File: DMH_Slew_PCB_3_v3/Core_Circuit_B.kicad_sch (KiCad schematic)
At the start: 60 parts, among them J21 Conn_02x03_Top_Bottom, J22 Conn_02x06_Top_Bottom, J23 Conn_02x03_Top_Bottom, J24 Conn_02x03_Top_Bottom, J25 Conn_02x06_Top_Bottom, J26 Conn_02x03_Top_Bottom, J27 Conn_01x08, J28 Conn_01x08, J29 Conn_01x08, J30 Conn_01x08, J6 TS_Jack_6.35mm_Sw, J7 TS_Jack_6.35mm_Sw, J8 TS_Jack_6.35mm_Sw, Q10 BC558, Q7 BC548, Q8 BC548, Q9 BC558, SW4 SW_DPDT_3way, SW5 SW_DPDT, SW6 SPDT_OnOffOn, U3 TL074, U4 TL074

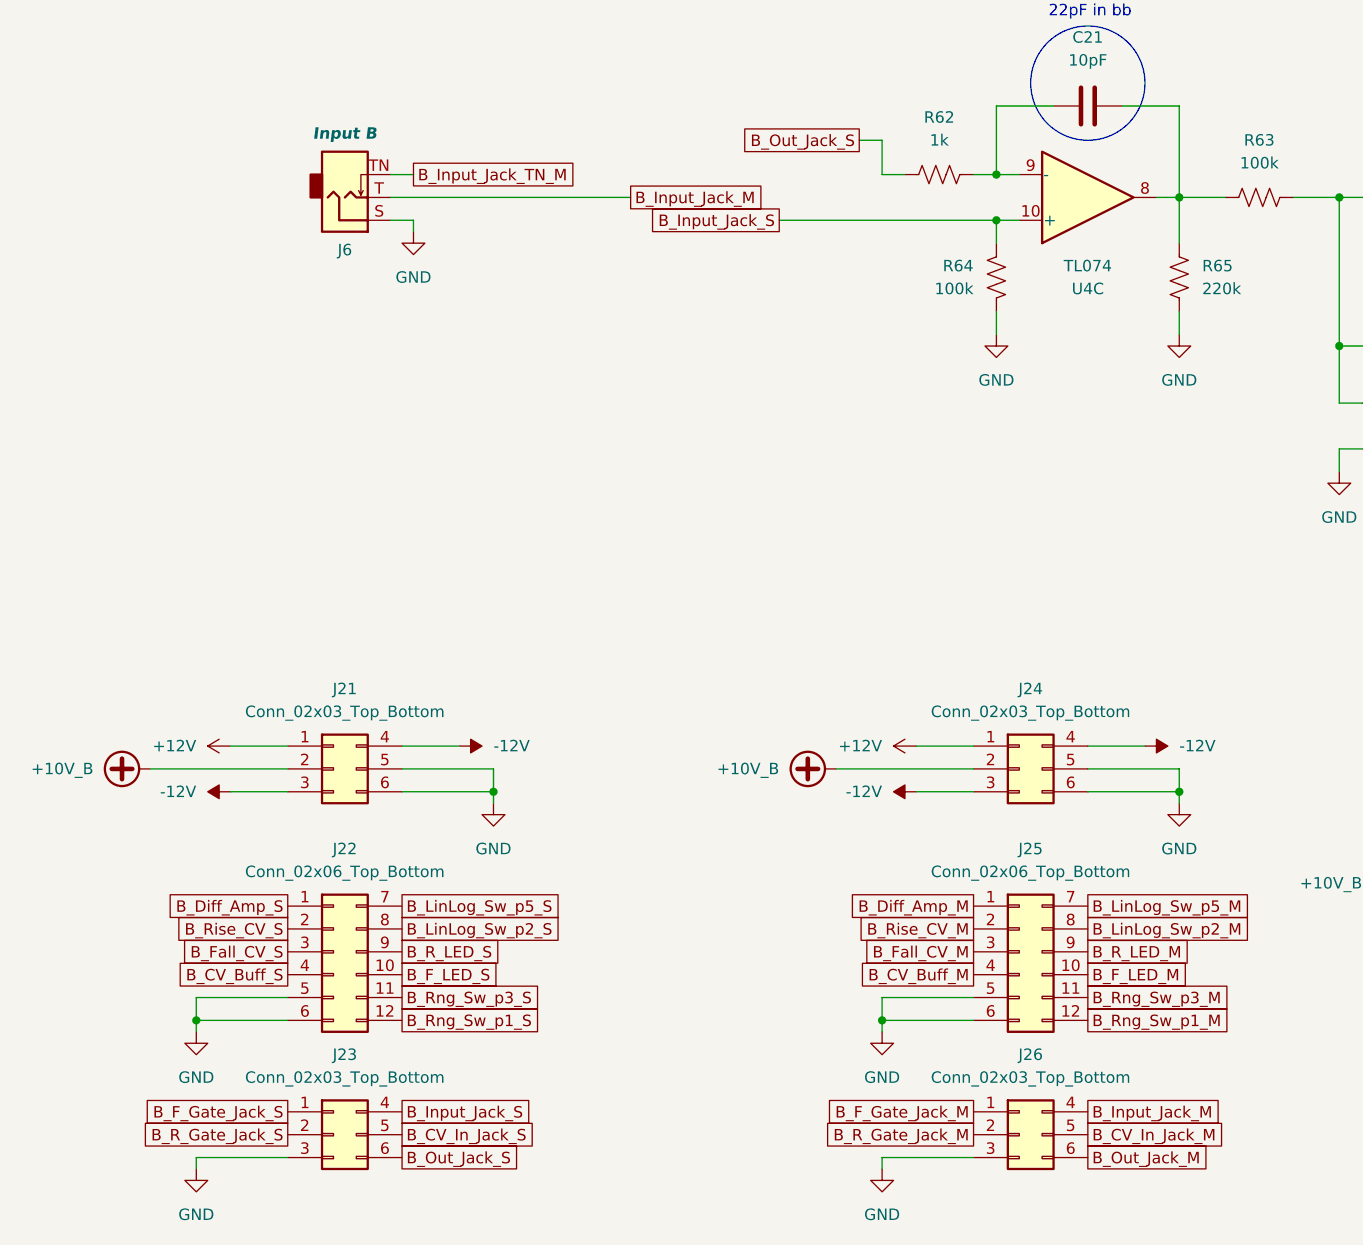
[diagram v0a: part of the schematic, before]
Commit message: Exposed loopback resistor to submodule connector
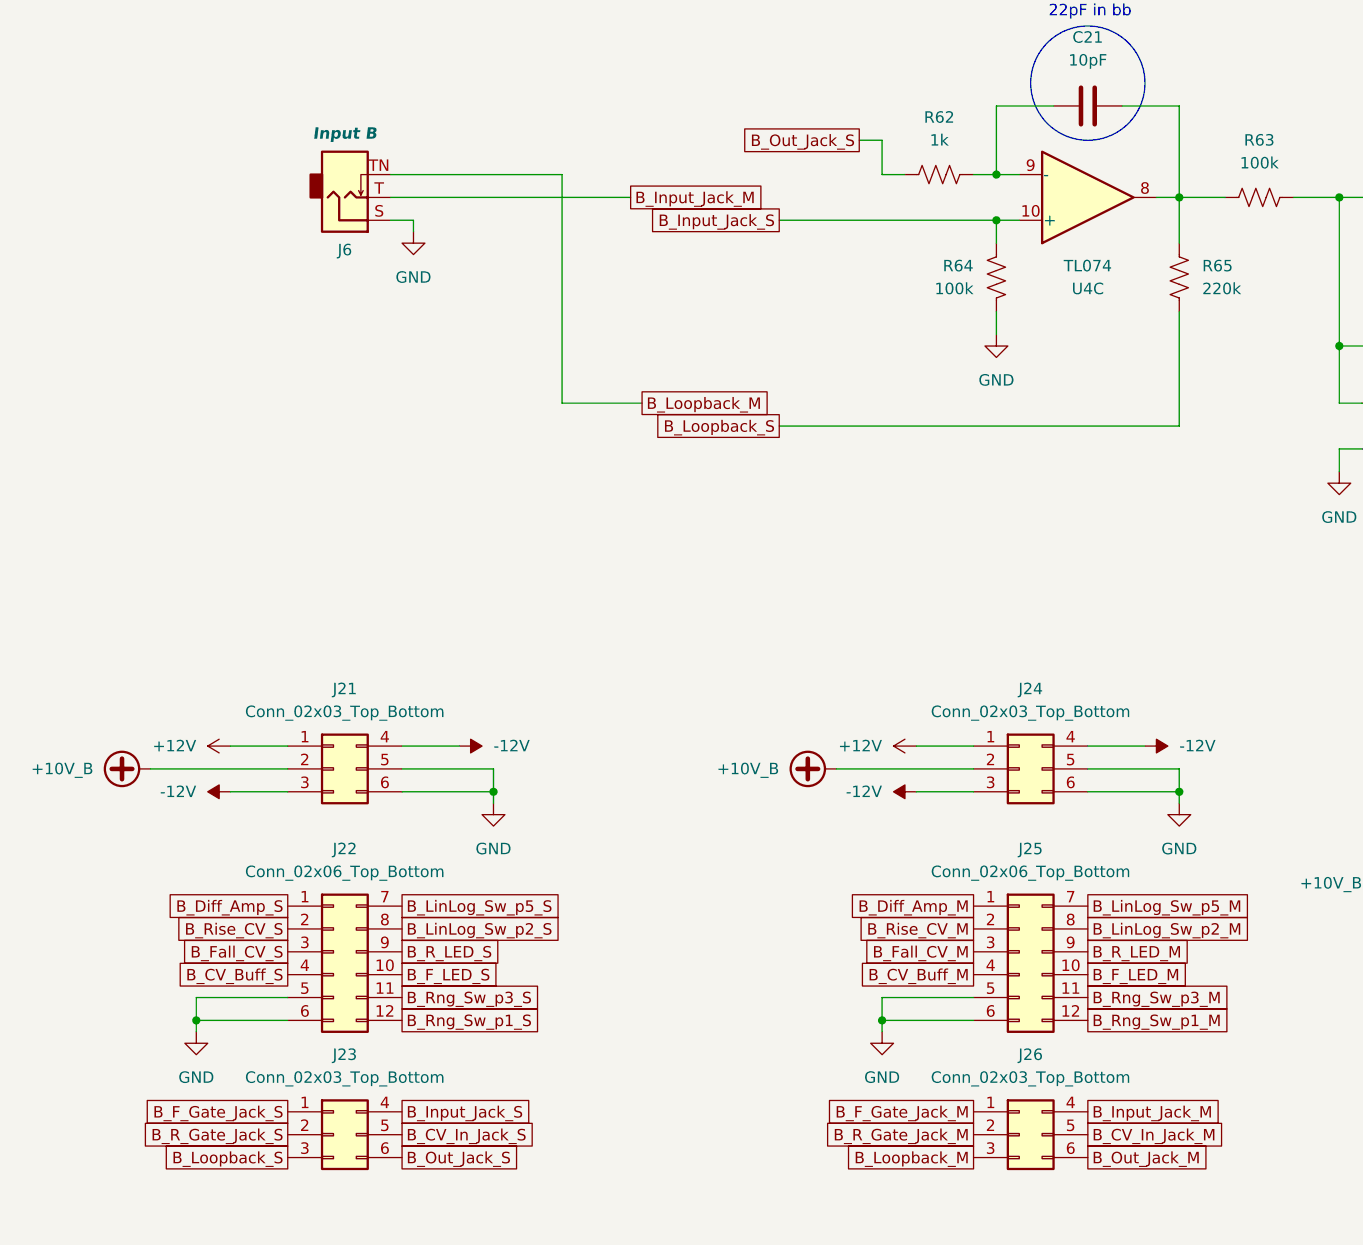
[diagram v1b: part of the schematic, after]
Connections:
- net GND: no longer J23.3 (Pin_3), J26.3 (Pin_3), R65.2
- net B_Input_Jack_TN_M renamed B_Loopback_M
- net B_Loopback_M: now also J26.3 (Pin_3)
- new net B_Loopback_S: J23.3 (Pin_3), R65.2
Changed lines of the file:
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@@
 	(wire
 		(pts
-			(xy 110.49 271.78) (xy 110.49 273.05)
-		)
-		(stroke
-			(width 0)
-			(type default)
-		)
-	)
-	(wire
-		(pts
 			(xy 322.58 132.08) (xy 323.85 132.08)
 		)
@@
 	(wire
 		(pts
+			(xy 74.93 162.56) (xy 74.93 187.96)
+		)
+		(stroke
+			(width 0)
+			(type default)
+		)
+	)
+	(wire
+		(pts
 			(xy 147.32 87.63) (xy 154.94 87.63)
 		)
@@
 	(wire
 		(pts
-			(xy 34.29 271.78) (xy 34.29 273.05)
-		)
-		(stroke
-			(width 0)
-			(type default)
-		)
-	)
-	(wire
-		(pts
 			(xy 123.19 177.8) (xy 123.19 180.34)
 		)
@@
 	(wire
 		(pts
-			(xy 55.88 162.56) (xy 58.42 162.56)
+			(xy 55.88 162.56) (xy 74.93 162.56)
 		)
 		(stroke
@@
 	(wire
 		(pts
+			(xy 74.93 187.96) (xy 83.82 187.96)
+		)
+		(stroke
+			(width 0)
+			(type default)
+		)
+	)
+	(wire
+		(pts
 			(xy 323.85 132.08) (xy 323.85 148.59)
 		)
@@
 	(wire
 		(pts
-			(xy 143.51 177.8) (xy 143.51 180.34)
+			(xy 143.51 177.8) (xy 143.51 190.5)
 		)
 		(stroke
@@
 	(wire
 		(pts
-			(xy 120.65 271.78) (xy 110.49 271.78)
-		)
-		(stroke
-			(width 0)
-			(type default)
-		)
-	)
-	(wire
-		(pts
 			(xy 233.68 158.75) (xy 242.57 158.75)
 		)
@@
 	(wire
 		(pts
-			(xy 44.45 271.78) (xy 34.29 271.78)
-		)
-		(stroke
-			(width 0)
-			(type default)
-		)
-	)
-	(wire
-		(pts
 			(xy 252.73 163.83) (xy 250.19 163.83)
 		)
@@
 	(wire
 		(pts
+			(xy 99.06 190.5) (xy 143.51 190.5)
+		)
+		(stroke
+			(width 0)
+			(type default)
+		)
+	)
+	(wire
+		(pts
 			(xy 177.8 220.98) (xy 177.8 223.52)
 		)
@@
 		)
 	)
-	(global_label "B_Input_Jack_TN_M"
-		(shape passive)
-		(at 58.42 162.56 0)
-		(fields_autoplaced yes)
-		(effects
-			(font
-				(size 1.27 1.27)
-			)
-			(justify left)
-		)
-		(property "Intersheetrefs" "${INTERSHEET_REFS}"
-			(at 79.3059 162.56 0)
-			(effects
-				(font
-					(size 1.27 1.27)
-				)
-				(justify left)
-				(hide yes)
-			)
-		)
-	)
 	(global_label "B_LinLog_Sw_p5_S"
 		(shape passive)
@@
 		)
 	)
+	(global_label "B_Loopback_S"
+		(shape passive)
+		(at 99.06 190.5 180)
+		(fields_autoplaced yes)
+		(effects
+			(font
+				(size 1.27 1.27)
+			)
+			(justify right)
+		)
+		(property "Intersheetrefs" "${INTERSHEET_REFS}"
+			(at 83.8816 190.5 0)
+			(effects
+				(font
+					(size 1.27 1.27)
+				)
+				(justify right)
+				(hide yes)
+			)
+		)
+	)
 	(global_label "B_CV_In_Jack_M"
 		(shape passive)
@@
 		)
 	)
+	(global_label "B_Loopback_M"
+		(shape passive)
+		(at 83.82 187.96 0)
+		(fields_autoplaced yes)
+		(effects
+			(font
+				(size 1.27 1.27)
+			)
+			(justify left)
+		)
+		(property "Intersheetrefs" "${INTERSHEET_REFS}"
+			(at 99.2403 187.96 0)
+			(effects
+				(font
+					(size 1.27 1.27)
+				)
+				(justify left)
+				(hide yes)
+			)
+		)
+	)
 	(global_label "B_Rng_Sw_p1_S"
 		(shape passive)
@@
 		)
 	)
+	(global_label "B_Loopback_S"
+		(shape passive)
+		(at 44.45 271.78 180)
+		(fields_autoplaced yes)
+		(effects
+			(font
+				(size 1.27 1.27)
+			)
+			(justify right)
+		)
+		(property "Intersheetrefs" "${INTERSHEET_REFS}"
+			(at 29.2716 271.78 0)
+			(effects
+				(font
+					(size 1.27 1.27)
+				)
+				(justify right)
+				(hide yes)
+			)
+		)
+	)
 	(global_label "B_LinLog_Sw_p2_M"
 		(shape passive)
@@
 		)
 	)
+	(global_label "B_Loopback_M"
+		(shape passive)
+		(at 120.65 271.78 180)
+		(fields_autoplaced yes)
+		(effects
+			(font
+				(size 1.27 1.27)
+			)
+			(justify right)
+		)
+		(property "Intersheetrefs" "${INTERSHEET_REFS}"
+			(at 105.2297 271.78 0)
+			(effects
+				(font
+					(size 1.27 1.27)
+				)
+				(justify right)
+				(hide yes)
+			)
+		)
+	)
 	(global_label "B_Out_Jack_M"
 		(shape passive)
@@
 		(polyline
 			(pts
-				(xy 44.45 152.4) (xy 80.01 152.4) (xy 80.01 177.8) (xy 44.45 177.8)
+				(xy 44.45 152.4) (xy 80.01 152.4) (xy 80.01 198.12) (xy 44.45 198.12)
 			)
 			(stroke
@@
 	)
 	(symbol
-		(lib_id "power:GND")
-		(at 34.29 273.05 0)
-		(mirror y)
-		(unit 1)
-		(exclude_from_sim no)
-		(in_bom yes)
-		(on_board yes)
-		(dnp no)
-		(fields_autoplaced yes)
-		(property "Reference" "#PWR0108"
-			(at 34.29 279.4 0)
-			(effects
-				(font
-					(size 1.27 1.27)
-				)
-				(hide yes)
-			)
-		)
-		(property "Value" "GND"
-			(at 34.29 278.13 0)
-			(effects
-				(font
-					(size 1.27 1.27)
-				)
-			)
-		)
-		(property "Footprint" ""
-			(at 34.29 273.05 0)
-			(effects
-				(font
-					(size 1.27 1.27)
-				)
-				(hide yes)
-			)
-		)
-		(property "Datasheet" ""
-			(at 34.29 273.05 0)
-			(effects
-				(font
-					(size 1.27 1.27)
-				)
-				(hide yes)
-			)
-		)
-		(property "Description" "Power symbol creates a global label with name \"GND\" , ground"
-			(at 34.29 273.05 0)
-			(effects
-				(font
-					(size 1.27 1.27)
-				)
-				(hide yes)
-			)
-		)
-		(pin "1"
-		)
-		(instances
-			(project "DMH_Slew_PCB_1_v3"
-				(path "/58f4306d-5387-4983-bb08-41a2313fd315/77d402a4-d1d6-4e9c-af86-3ca5793147b8"
-					(reference "#PWR0108")
-					(unit 1)
-				)
-			)
-		)
-	)
-	(symbol
 		(lib_id "Device:R_US")
 		(at 381 90.17 270)
@@
 	(symbol
 		(lib_id "power:GND")
-		(at 110.49 273.05 0)
-		(mirror y)
-		(unit 1)
-		(exclude_from_sim no)
-		(in_bom yes)
-		(on_board no)
-		(dnp no)
-		(fields_autoplaced yes)
-		(property "Reference" "#PWR0115"
-			(at 110.49 279.4 0)
-			(effects
-				(font
-					(size 1.27 1.27)
-				)
-				(hide yes)
-			)
-		)
-		(property "Value" "GND"
-			(at 110.49 278.13 0)
-			(effects
-				(font
-					(size 1.27 1.27)
-				)
-			)
-		)
-		(property "Footprint" ""
-			(at 110.49 273.05 0)
-			(effects
-				(font
-					(size 1.27 1.27)
-				)
-				(hide yes)
-			)
-		)
-		(property "Datasheet" ""
-			(at 110.49 273.05 0)
-			(effects
-				(font
-					(size 1.27 1.27)
-				)
-				(hide yes)
-			)
-		)
-		(property "Description" "Power symbol creates a global label with name \"GND\" , ground"
-			(at 110.49 273.05 0)
-			(effects
-				(font
-					(size 1.27 1.27)
-				)
-				(hide yes)
-			)
-		)
-		(pin "1"
-		)
-		(instances
-			(project "DMH_Slew_PCB_1_v3"
-				(path "/58f4306d-5387-4983-bb08-41a2313fd315/77d402a4-d1d6-4e9c-af86-3ca5793147b8"
-					(reference "#PWR0115")
-					(unit 1)
-				)
-			)
-		)
-	)
-	(symbol
-		(lib_id "power:GND")
 		(at 266.7 101.6 0)
 		(unit 1)
@@
 					(unit 1)
 				)
-			)
-		)
-	)
-	(symbol
-		(lib_id "power:GND")
-		(at 143.51 180.34 0)
-		(unit 1)
-		(exclude_from_sim no)
-		(in_bom yes)
-		(on_board yes)
-		(dnp no)
-		(fields_autoplaced yes)
-		(property "Reference" "#PWR064"
-			(at 143.51 186.69 0)
-			(effects
-				(font
-					(size 1.27 1.27)
-				)
-				(hide yes)
-			)
-		)
-		(property "Value" "GND"
-			(at 143.51 185.42 0)
-			(effects
-				(font
-					(size 1.27 1.27)
-				)
-			)
-		)
-		(property "Footprint" ""
-			(at 143.51 180.34 0)
-			(effects
-				(font
-					(size 1.27 1.27)
-				)
-				(hide yes)
-			)
-		)
-		(property "Datasheet" ""
-			(at 143.51 180.34 0)
-			(effects
-				(font
-					(size 1.27 1.27)
-				)
-				(hide yes)
-			)
-		)
-		(property "Description" "Power symbol creates a global label with name \"GND\" , ground"
-			(at 143.51 180.34 0)
-			(effects
-				(font
-					(size 1.27 1.27)
-				)
-				(hide yes)
-			)
-		)
-		(pin "1"
-		)
-		(instances
-			(project "DMH_Slew_PCB_1_v3"
-				(path "/58f4306d-5387-4983-bb08-41a2313fd315/77d402a4-d1d6-4e9c-af86-3ca5793147b8"
-					(reference "#PWR064")
-					(unit 1)
-				)

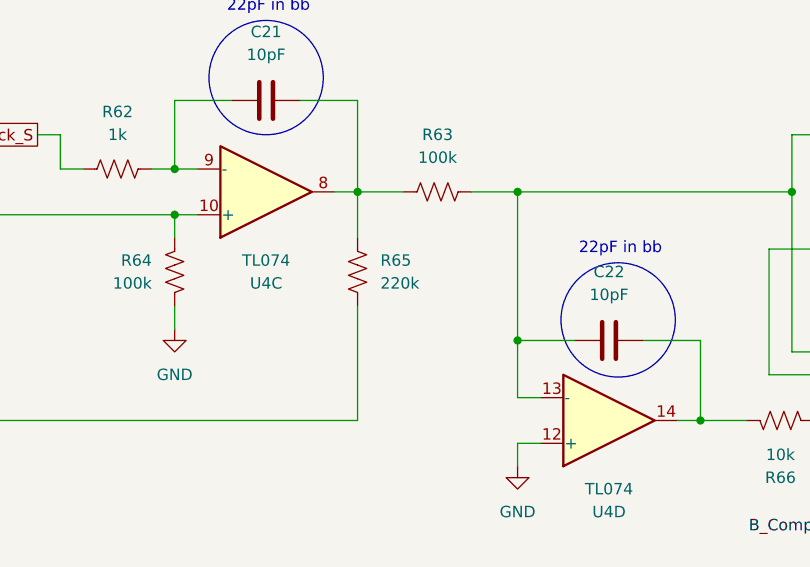
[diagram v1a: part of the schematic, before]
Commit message: Changed loopback resistor to 82k
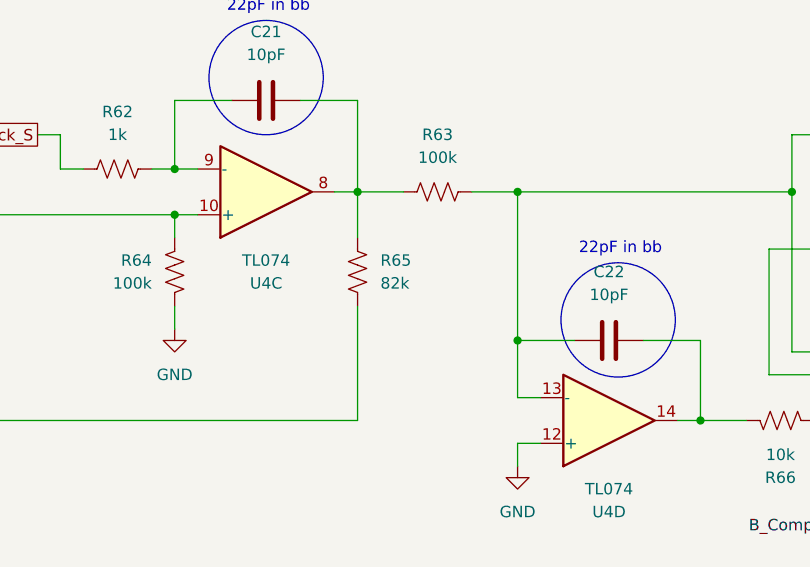
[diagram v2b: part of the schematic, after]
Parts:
- R65: value 220k -> 82k
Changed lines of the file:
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@@
 			)
 		)
-		(property "Value" "220k"
+		(property "Value" "82k"
 			(at 146.05 175.2599 0)
 			(effects
